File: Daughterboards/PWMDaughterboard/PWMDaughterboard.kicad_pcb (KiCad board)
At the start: 2 copper layers, 49 x 38 mm, 15 parts, among them J1 Conn_01x10, J10 Conn_01x02, J11 Conn_01x02, J12 Conn_01x02, J13 Conn_01x02, J2 Conn_01x04, J3 Conn_01x02, J4 Conn_01x02, J5 Conn_01x02, J6 Conn_01x02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

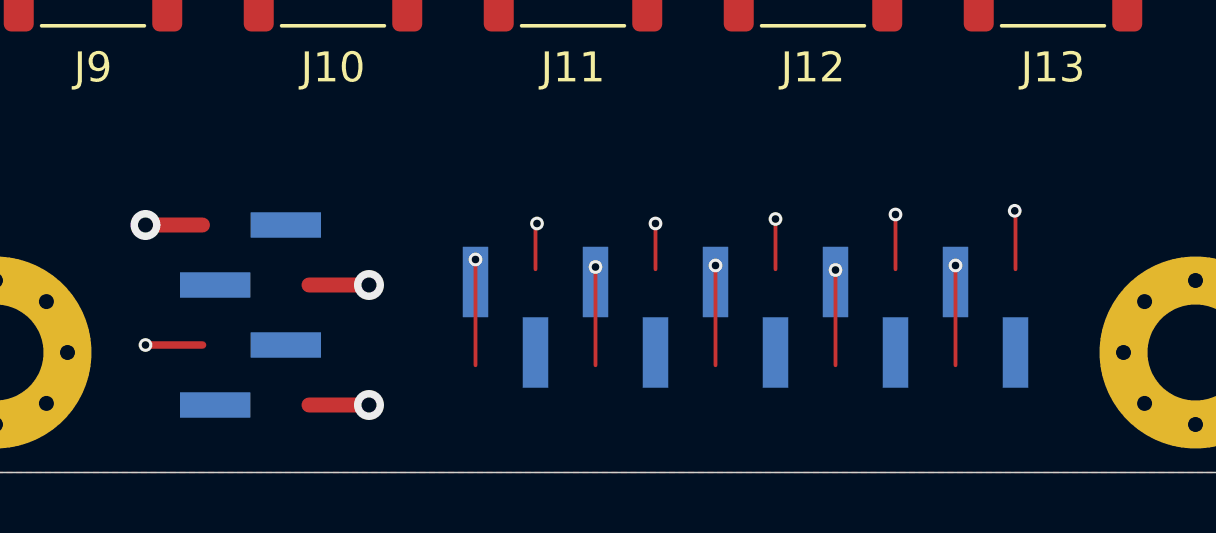
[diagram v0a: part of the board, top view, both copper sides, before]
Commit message: Switched SMD headers J1,2 to through-hole
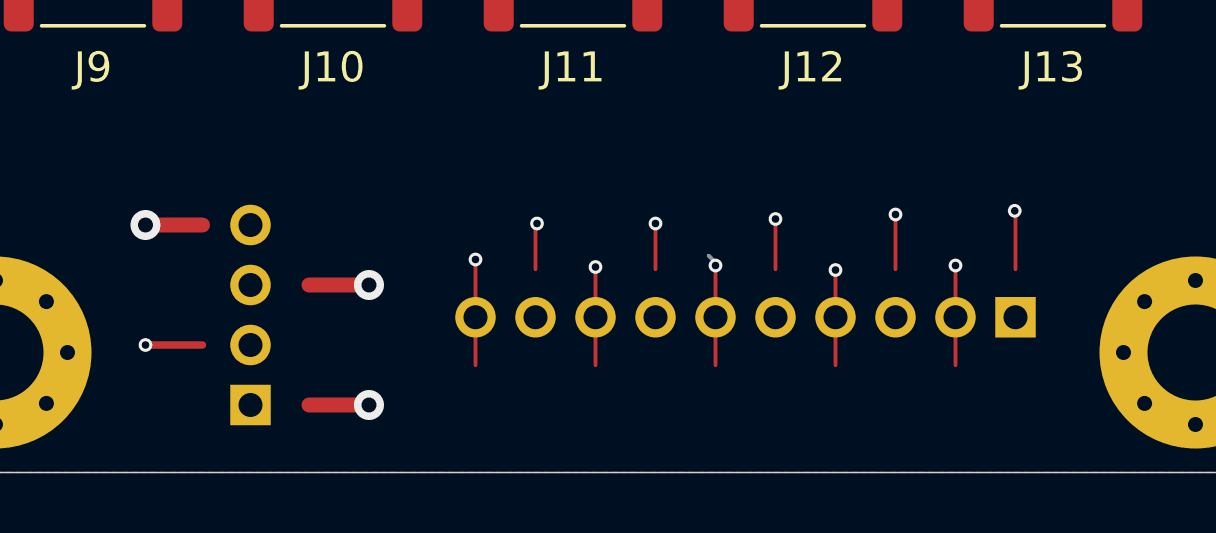
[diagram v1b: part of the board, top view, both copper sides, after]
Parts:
- J1: footprint Connector_PinHeader_2.00mm:PinHeader_1x10_P2.00mm_Vertical_SMD_Pin1Left -> Connector_PinHeader_2.00mm:PinHeader_1x10_P2.00mm_Vertical
- J2: footprint Connector_PinHeader_2.00mm:PinHeader_1x04_P2.00mm_Vertical_SMD_Pin1Left -> Connector_PinHeader_2.00mm:PinHeader_1x04_P2.00mm_Vertical
- moved J1 9.00 mm to (153.8, 108.3), turned to 90 degrees
- moved J2 3.00 mm to (128.2, 111.2)
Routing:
- net /PWM5: track 0.00 -> 4.00 mm, vias 0 -> 1
- net /PWM4: track 5.85 -> 1.85 mm, vias 2 -> 1
- net /PWM9: track 0.00 -> 3.67 mm, vias 0 -> 1
- net /PWM0: track 5.63 -> 1.96 mm, vias 2 -> 1
- net /PWM8: track 4.87 -> 1.55 mm, vias 2 -> 1
- net /PWM1: track 0.00 -> 3.33 mm, vias 0 -> 1
- net /PWM7: track 0.00 -> 3.27 mm, vias 0 -> 1
- net /PWM2: track 5.10 -> 1.82 mm, vias 2 -> 1
- net /PWM6: track 4.85 -> 1.67 mm, vias 2 -> 1
- net /PWM3: track 0.00 -> 3.17 mm, vias 0 -> 1

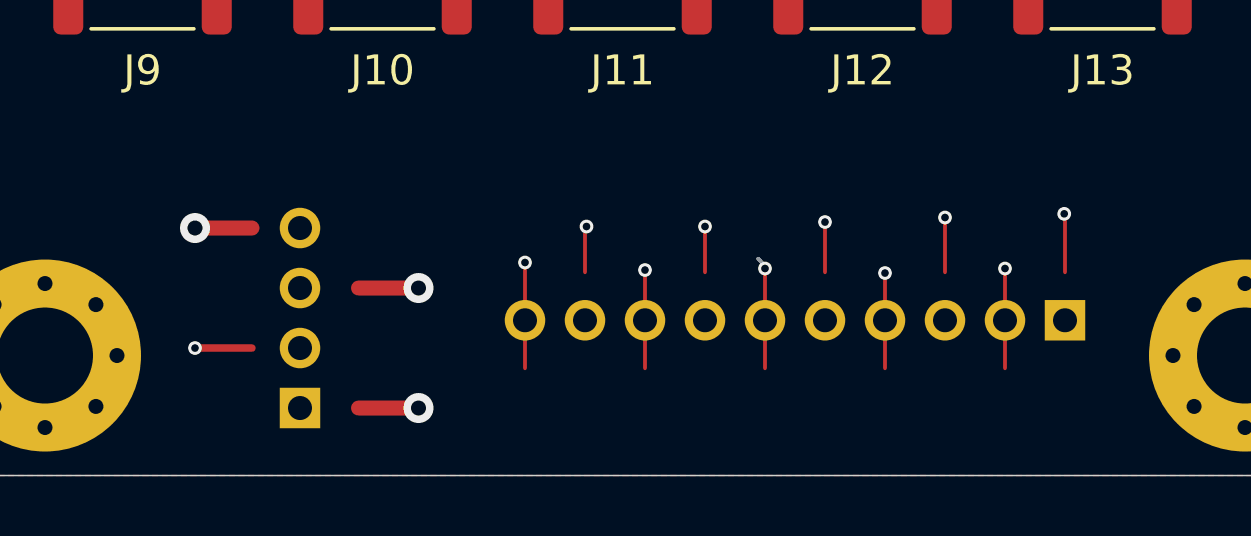
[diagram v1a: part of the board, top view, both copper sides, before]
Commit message: cleaned up vias
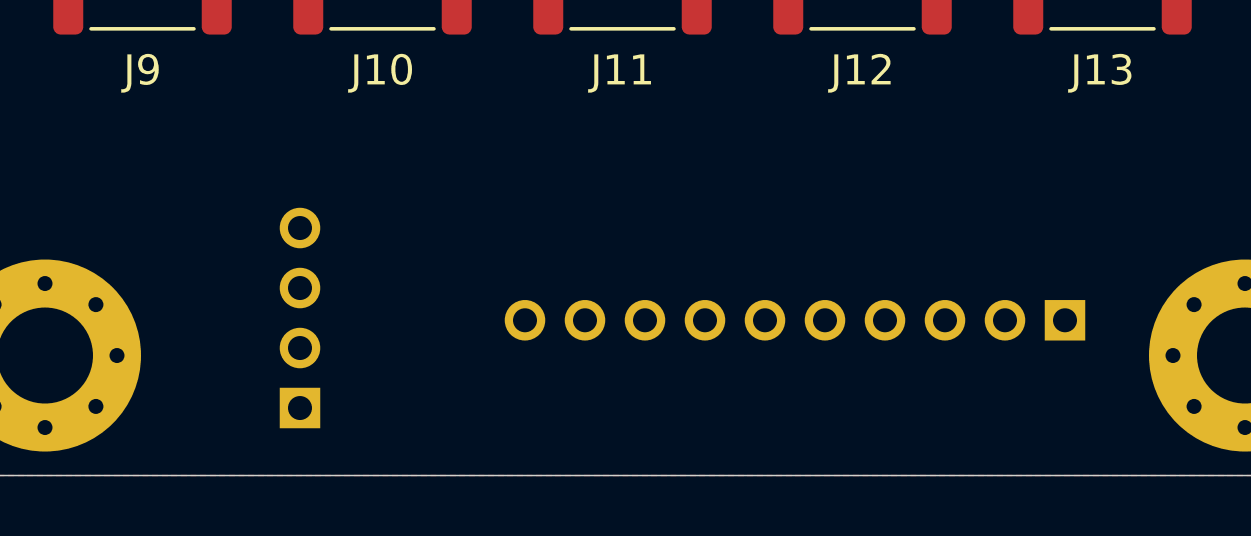
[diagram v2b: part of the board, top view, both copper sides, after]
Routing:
- net /PWM5: track 4.00 -> 0.00 mm, vias 1 -> 0
- net GND: track 3.90 -> 0.00 mm, vias 2 -> 0
- net /PWM9: track 3.67 -> 0.00 mm, vias 1 -> 0
- net /PWM1: track 3.33 -> 0.00 mm, vias 1 -> 0
- net /PWM7: track 3.27 -> 0.00 mm, vias 1 -> 0
- net /PWM3: track 3.17 -> 0.00 mm, vias 1 -> 0
- net +3V3: track 2.00 -> 0.00 mm, vias 1 -> 0
- net /PWM0: track 1.96 -> 0.00 mm, vias 1 -> 0
- net VBUS: track 1.90 -> 0.00 mm, vias 1 -> 0
- net /PWM4: track 1.85 -> 0.00 mm, vias 1 -> 0
- net /PWM2: track 1.82 -> 0.00 mm, vias 1 -> 0
- net /PWM6: track 1.67 -> 0.00 mm, vias 1 -> 0
- net /PWM8: track 1.55 -> 0.00 mm, vias 1 -> 0

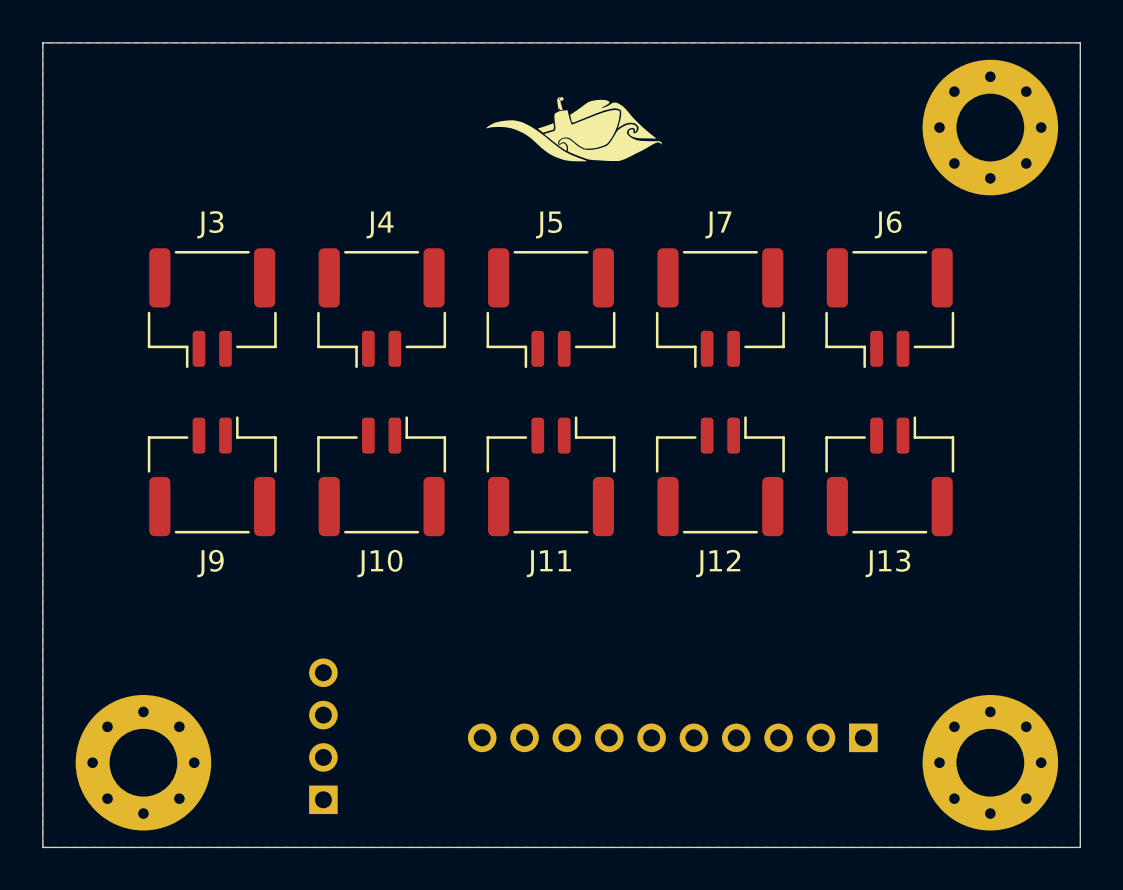
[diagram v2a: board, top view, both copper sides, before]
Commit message: Added traces
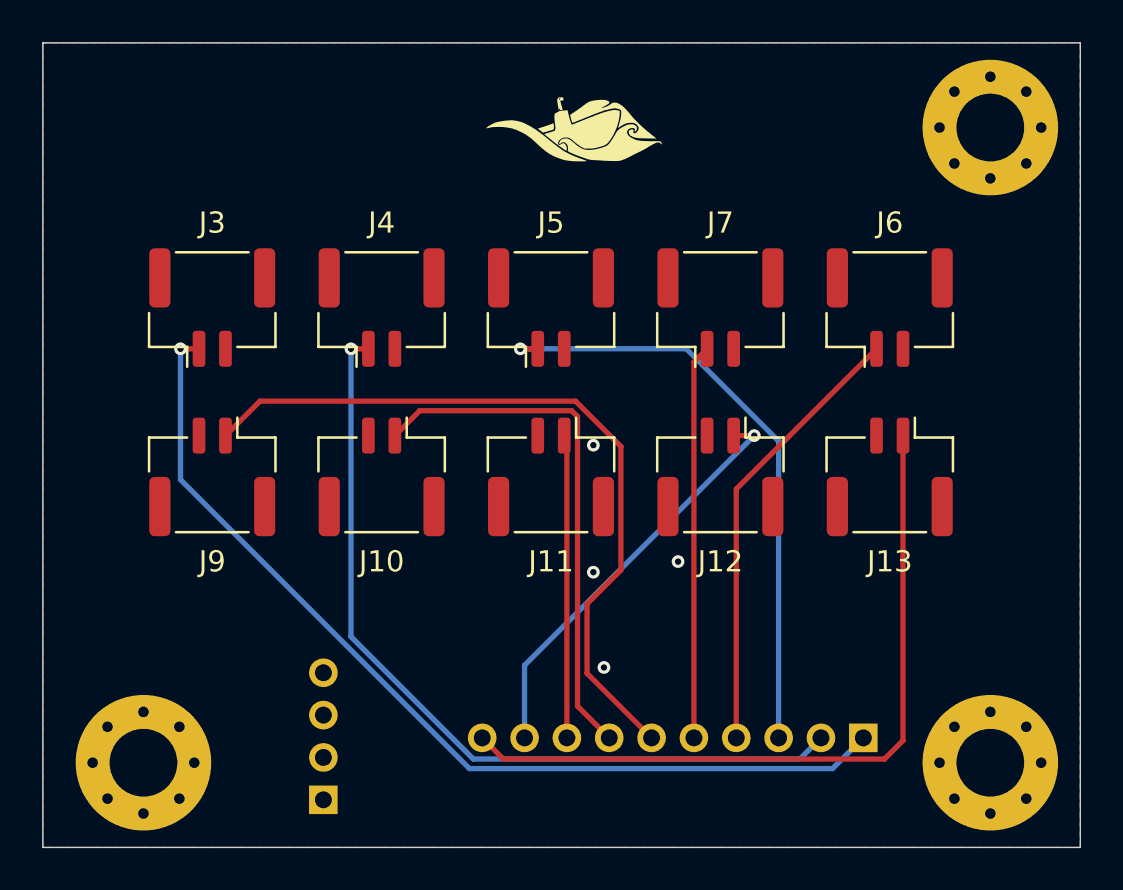
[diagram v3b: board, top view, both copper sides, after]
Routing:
- net /PWM0: track 0.00 -> 45.6 mm, vias 0 -> 1
- net /PWM1: track 0.00 -> 39.4 mm, vias 0 -> 1
- net /PWM5: track 0.00 -> 35.9 mm
- net /PWM9: track 0.00 -> 35.1 mm
- net /PWM2: track 0.00 -> 28.8 mm, vias 0 -> 1
- net /PWM6: track 0.00 -> 25.0 mm
- net /PWM3: track 0.00 -> 21.1 mm
- net /PWM8: track 0.00 -> 19.7 mm, vias 0 -> 1
- net /PWM4: track 0.00 -> 18.6 mm
- net /PWM7: track 0.00 -> 14.3 mm
- net GND: vias 0 -> 4
- added copper zone on B.Cu, net GND

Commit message: Added silkscreen
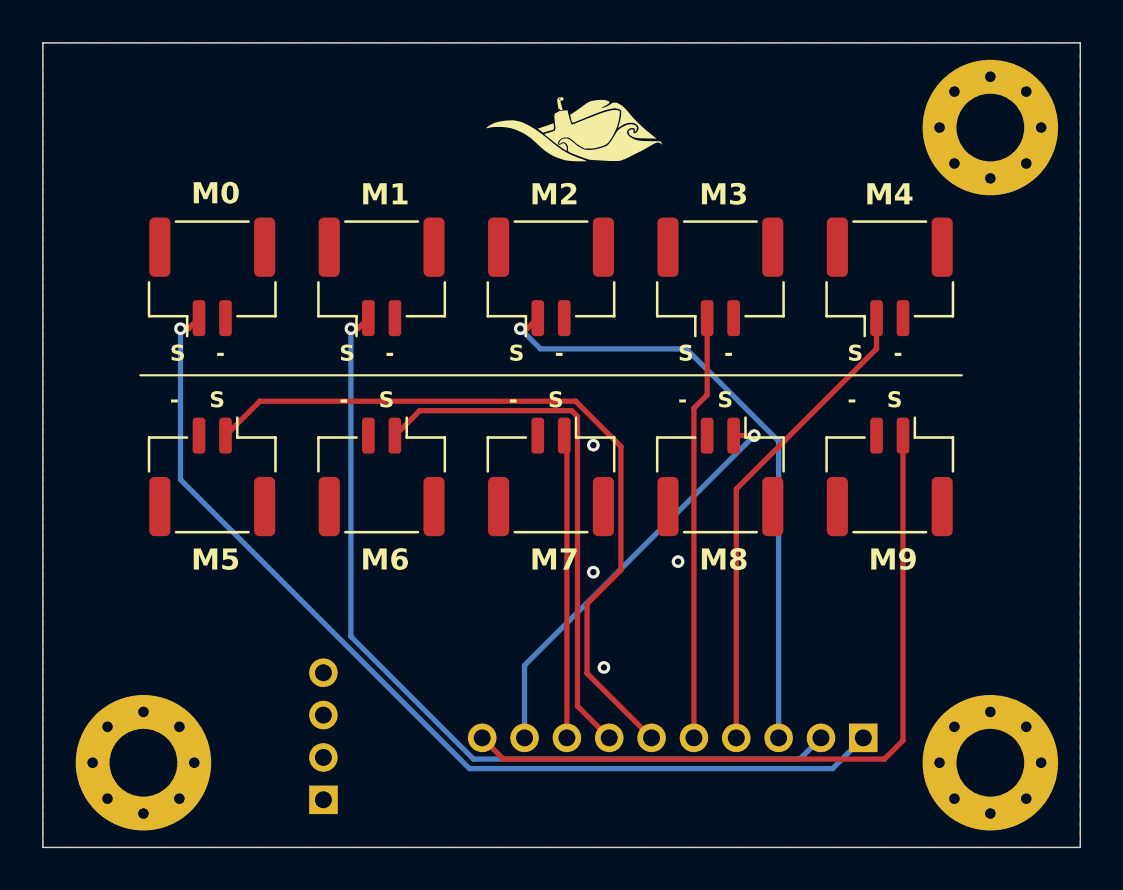
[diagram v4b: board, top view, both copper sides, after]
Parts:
- moved J3 1.45 mm to (123.0, 86.5)
- moved J4 1.45 mm to (131.0, 86.5)
- moved J5 1.45 mm to (139.0, 86.5)
- moved J6 1.45 mm to (155.0, 86.5)
- moved J7 1.45 mm to (147.0, 86.5)
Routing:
- net /PWM4: track 18.6 -> 20.1 mm
- net /PWM3: track 21.1 -> 22.6 mm
- net /PWM1: track 39.4 -> 40.6 mm
- net /PWM0: track 45.6 -> 46.7 mm
- net /PWM2: track 28.8 -> 29.4 mm
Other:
- board text added: "- S"
- board text added: "M0"
- board text added: "M1"
- board text added: "M2"
- board text added: "M3"
- board text added: "M4"
- board text added: "M5"
- board text added: "M6"
- board text added: "M7"
- board text added: "M8"
- board text added: "M9"
- board text added: "S -"
